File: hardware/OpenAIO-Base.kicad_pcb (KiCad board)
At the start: 6 copper layers, 35 x 35 mm, 341 parts, among them J15 5V, J16 5V, J17 5V, J18 5V, J20 5V, J21 5V, J23 5V, J24 5V, J25 5V, J26 5V, J27 5V, J28 5V, J29 5V, J30 5V, J31 5V, J32 5V, J33 5V, J34 5V, J35 5V, J37 5V, J38 5V, J39 5V, J40 5V, J41 5V, J42 5V, J43 5V, J44 5V, J45 5V, J48 5V, J49 5V, J50 5V, J51 5V, J52 5V, J53 5V, J54 5V, J55 5V, J90 Core_LGA, J91 Core_LGA, Q1 AP1606, Q10 DOY180N03T, Q11 DOY180N03T, Q12 DOY180N03T, Q13 DOY180N03T, Q14 DOY180N03T, Q15 DOY180N03T, Q16 DOY180N03T, Q17 DOY180N03T, Q18 DOY180N03T, Q19 DOY180N03T, Q2 AP1606, Q20 DOY180N03T, Q21 DOY180N03T, Q22 DOY180N03T, Q23 DOY180N03T, Q24 DOY180N03T, Q25 DOY180N03T, Q26 DOY180N03T, Q3 DOY180N03T, Q4 DOY180N03T, Q5 DOY180N03T, Q6 DOY180N03T, Q7 DOY180N03T, Q8 DOY180N03T, Q9 DOY180N03T, U1 TS2306A 240GF MSM 9_C2976675, U10 COS8051SOT, U11 TLV7031DPWR, U12 SM06B-SRSS-TB(LF)(SN), U13 AT32F421G8U7, U14 NSG2065Q, U15 AT32F421G8U7, U16 NSG2065Q, U17 AT32F421G8U7, U18 NSG2065Q, U19 AT32F421G8U7, U2 RP2354A, U20 NSG2065Q, U21 SX1281IMLTRT, U22 ESP32-C3, U23 TLV75533PDQNR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

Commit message: OpenAIO: two board projects from one schematic via the multiboard plugin, master PCB retired
OpenAIO.kicad_pro keeps the schematic; OpenAIO-Base and OpenAIO-Core are full
projects in the same directory, root schematic symlinked, seeded from the last
split of the master. Own design rules per board (Base 2 oz outer, Core 0.8 mm
1 oz, LGA-only bottom). tools/core_model.py exports the Core VRML/STEP as
J90's 3D model. split_boards, lga_place, lga_rule_area, core_outline and
lga_wire_root are gone with the master.

Co-Authored-By: Claude Fable 5 <noreply@anthropic.com>
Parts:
- removed C1, C11, C12, C13, C14, C2, C29, C30, C32, C34, C35, C5, C6, C7, C8, C9: 100n, Capacitor_SMD:C_0201_0603Metric
- removed C10, C4: 20p, Capacitor_SMD:C_0201_0603Metric
- removed C15, C16, C17, C25, C3: 4.7uF, Capacitor_SMD:C_0402_1005Metric
- removed C27: 22uF, Capacitor_SMD:C_0402_1005Metric
- removed C31: 470p, Capacitor_SMD:C_0201_0603Metric
- removed C33: 1uF, Capacitor_SMD:C_0402_1005Metric
- removed D1: LED_1_Blue, LED_SMD:LED_0402_1005Metric
- removed D7: LED_1_Green, LED_SMD:LED_0402_1005Metric
- removed D8: SDM02U30LP3-7B, lib:X3-DFN0603-2_L0.6-W0.3-RD
- removed J23, J26, J30, J34, J35, J37, J38, J39, J40, J41, J42, J43, J44, J45, J48, J49, J50, J51, J52, J53, J54, J55: 5V, lib:small_pad
- removed J91: Core_LGA, lib:Core_LGA_pads
- removed L1: AOTA-B201610S3R3-101-T, lib:IND-SMD_L2.0-W1.6_AOTA-B201610S3R3-101-T
- removed Q1, Q2: AP1606, lib:DFN-3L_L1.0-W0.6-P0.65-BR
- removed R1, R13: 100k, Resistor_SMD:R_0201_0603Metric
- removed R10, R8, R9: 30R, Resistor_SMD:R_0201_0603Metric
- removed R11, R12: 5.1k, Resistor_SMD:R_0201_0603Metric
- removed R14: 2.4k, Resistor_SMD:R_0201_0603Metric
- removed R15, R16, R26, R33: 75R, Resistor_SMD:R_0201_0603Metric
- removed R2, R25, R7: 10k, Resistor_SMD:R_0201_0603Metric
- removed R23: 6.49k, Resistor_SMD:R_0201_0603Metric
- removed R27: 3.9k, Resistor_SMD:R_0201_0603Metric
- removed R28: 12k, Resistor_SMD:R_0201_0603Metric
- removed R29: 1.4k, Resistor_SMD:R_0201_0603Metric
- removed R30: 680R, Resistor_SMD:R_0201_0603Metric
- removed R31, R32: 510R, Resistor_SMD:R_0201_0603Metric
- removed R5, R6: 1k, Resistor_SMD:R_0201_0603Metric
- removed U1: TS2306A 240GF MSM 9_C2976675, lib:SW-SMD_4P-L3.0-W2.0-P0.85-LS3.5
- removed U10: COS8051SOT, lib:SOT-23-5_L3.0-W1.7-P0.95-LS2.8-BR
- removed U11: TLV7031DPWR, lib:X2SON-4_L0.8-W0.8-P0.48-TL-A
- removed U2: RP2354A, lib:QFN-60_L7.0-W7.0-P0.40-TL-EP3.4
- removed U6: LP5912-1.8DRVR, lib:WSON-6-1EP_2x2mm_P0.65mm_EP1x1.6mm_ThermalVias
- removed U8: BMI270, lib:LGA-14_L3.0-W2.5-P0.50-BR
- removed U9: SN74LVC1G3157DTBR, lib:X2SON-6_L1.0-W0.8-BL
- removed X1: XTM25012000JT00351001, lib:CRYSTAL-SMD_4P-L2.5-W2.0-BL-A
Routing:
- net /OSD/VIDEO_IN: track 2.65 -> 0.00 mm
- net GND: track 20.3 -> 17.7 mm
- net /OSD/VID_FILT: track 2.57 -> 0.00 mm
- net /RP2354A/XIN: track 2.45 -> 0.00 mm
- net +3.3V: track 2.43 -> 0.00 mm
- net /OSD/VID_DC: track 1.47 -> 0.00 mm
- net Net-(C10-Pad2): track 0.88 -> 0.00 mm
- net /OSD/OSD_LVL: track 0.65 -> 0.00 mm
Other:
- board text added: "AIO"
- board text added: "Open"

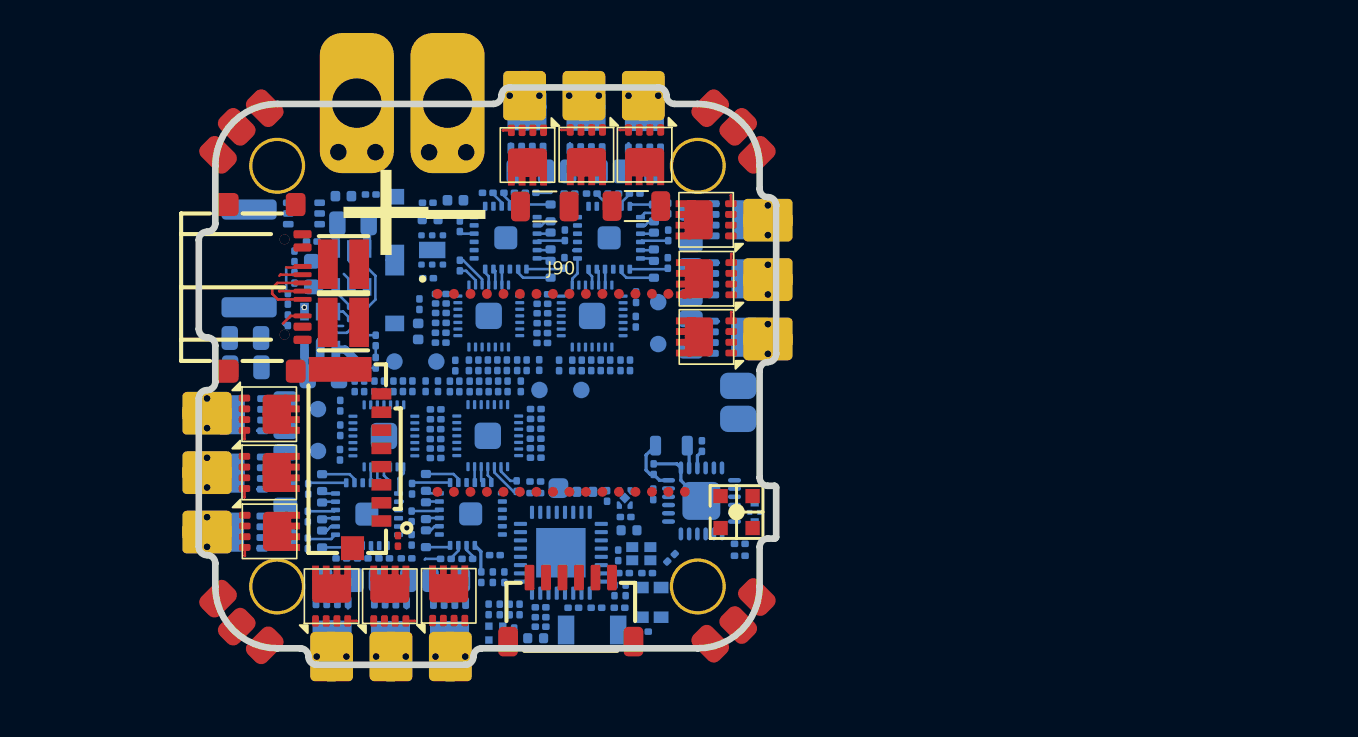
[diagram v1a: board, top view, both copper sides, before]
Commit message: OpenAIO: test points TP10-TP30 as LGA position markers (schematic + Base), project files as re-saved by KiCad
Co-Authored-By: Claude Fable 5 <noreply@anthropic.com>
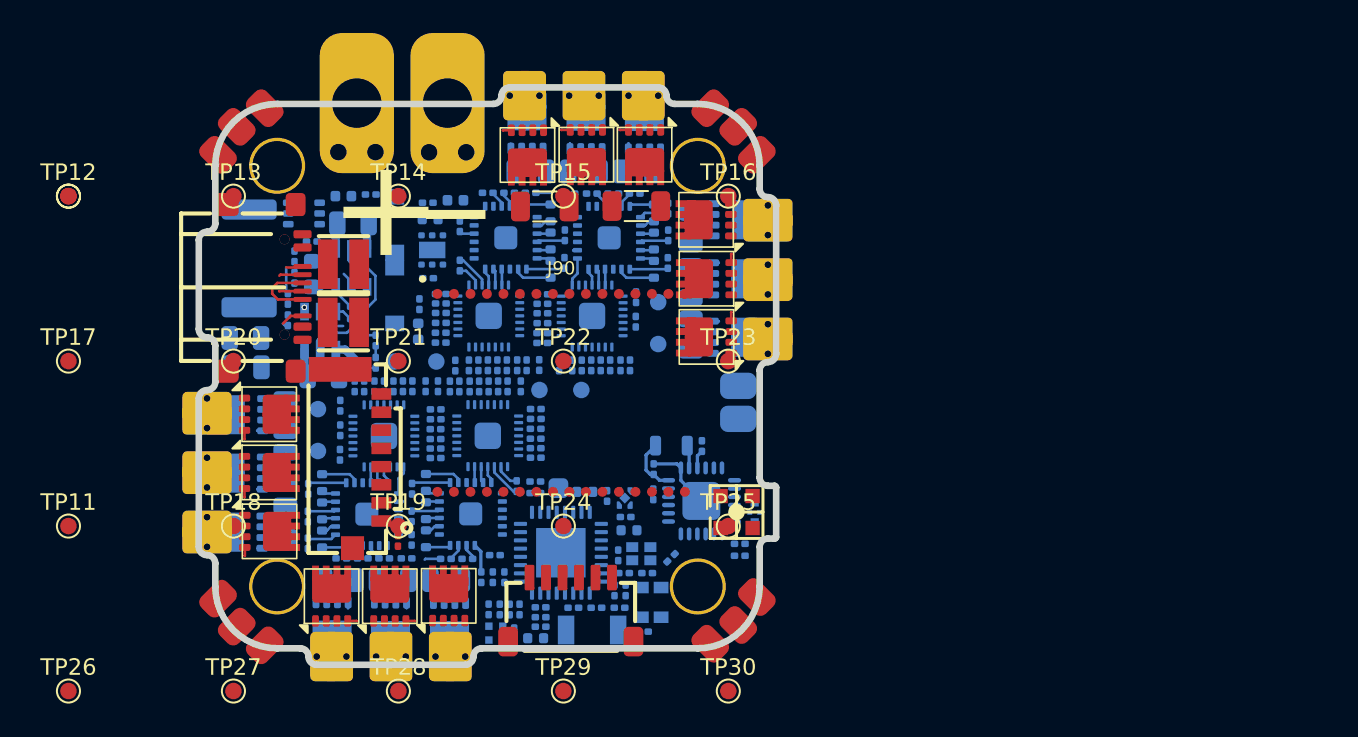
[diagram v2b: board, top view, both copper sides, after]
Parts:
- added TP10: TestPoint, OpenDrone:TestPoint_Pad_D1.0mm, F.Cu at (50.0, 50.0)
- added TP11: TestPoint, TestPoint:TestPoint_Pad_D1.0mm, F.Cu at (50.0, 70.0)
- added TP12: TestPoint, TestPoint:TestPoint_Pad_D1.0mm, F.Cu at (50.0, 50.0)
- added TP13: TestPoint, TestPoint:TestPoint_Pad_D1.0mm, F.Cu at (60.0, 50.0)
- added TP14: TestPoint, TestPoint:TestPoint_Pad_D1.0mm, F.Cu at (70.0, 50.0)
- added TP15: TestPoint, TestPoint:TestPoint_Pad_D1.0mm, F.Cu at (80.0, 50.0)
- added TP16: TestPoint, TestPoint:TestPoint_Pad_D1.0mm, F.Cu at (90.0, 50.0)
- added TP17: TestPoint, TestPoint:TestPoint_Pad_D1.0mm, F.Cu at (50.0, 60.0)
- added TP18: TestPoint, TestPoint:TestPoint_Pad_D1.0mm, F.Cu at (60.0, 70.0)
- added TP19: TestPoint, TestPoint:TestPoint_Pad_D1.0mm, F.Cu at (70.0, 70.0)
- added TP20: TestPoint, TestPoint:TestPoint_Pad_D1.0mm, F.Cu at (60.0, 60.0)
- added TP21: TestPoint, TestPoint:TestPoint_Pad_D1.0mm, F.Cu at (70.0, 60.0)
- added TP22: TestPoint, TestPoint:TestPoint_Pad_D1.0mm, F.Cu at (80.0, 60.0)
- added TP23: TestPoint, TestPoint:TestPoint_Pad_D1.0mm, F.Cu at (90.0, 60.0)
- added TP24: TestPoint, TestPoint:TestPoint_Pad_D1.0mm, F.Cu at (80.0, 70.0)
- added TP25: TestPoint, TestPoint:TestPoint_Pad_D1.0mm, F.Cu at (90.0, 70.0)
- added TP26: TestPoint, TestPoint:TestPoint_Pad_D1.0mm, F.Cu at (50.0, 80.0)
- added TP27: TestPoint, TestPoint:TestPoint_Pad_D1.0mm, F.Cu at (60.0, 80.0)
- added TP28: TestPoint, TestPoint:TestPoint_Pad_D1.0mm, F.Cu at (70.0, 80.0)
- added TP29: TestPoint, TestPoint:TestPoint_Pad_D1.0mm, F.Cu at (80.0, 80.0)
- added TP30: TestPoint, TestPoint:TestPoint_Pad_D1.0mm, F.Cu at (90.0, 80.0)

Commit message: OpenAIO: LGA pins from Stan's marker test points, 30 pads, J90/J91 regenerated and placed
lga_gen.py --from-base reads the marker test points on the Base (position +
net) into its pin table and generates footprints, symbol and interface
sheet; lga_apply.py replaces the markers with J90 at the pattern centre and
J91 on the Core, marks the marker symbols exclude-from-board and adds the
LED_STRIP global label on the root (it now crosses the LGA). Plugin update
assigned all 30 pad nets on both boards.

Co-Authored-By: Claude Fable 5 <noreply@anthropic.com>
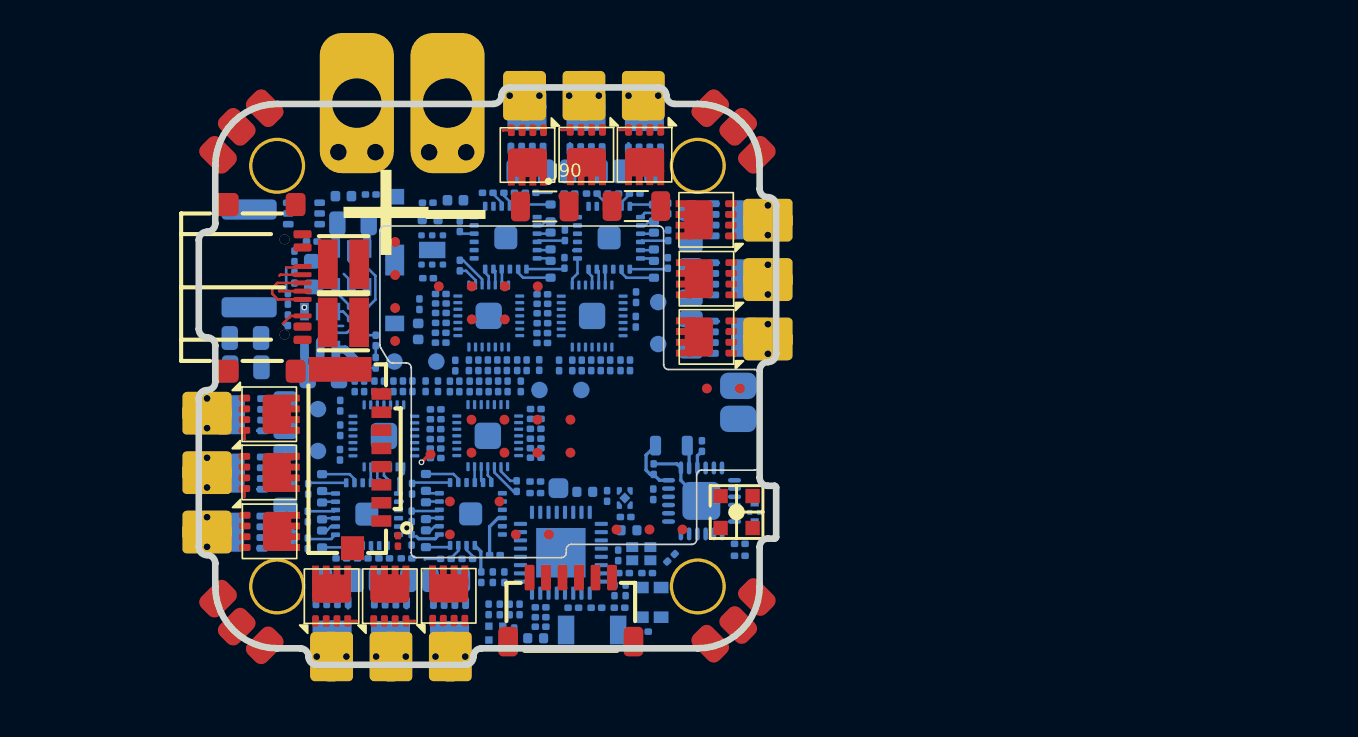
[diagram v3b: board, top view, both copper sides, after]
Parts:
- removed TP10: TestPoint, OpenDrone:TestPoint_Pad_D1.0mm
- removed TP11, TP12, TP13, TP14, TP15, TP16, TP17, TP18, TP19, TP20, TP21, TP22, TP23, TP24, TP25, TP26, TP27, TP28, TP29, TP30: TestPoint, TestPoint:TestPoint_Pad_D1.0mm
- moved J90 1.71 mm to (80.2, 60.3)
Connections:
- J20 pad 1: /Pads/LED_STRIP -> LED_STRIP
- J21 pad 1: /Pads/LED_STRIP -> LED_STRIP
- J31 pad 1: /Pads/LED_STRIP -> LED_STRIP
- J32 pad 1: /Pads/LED_STRIP -> LED_STRIP
- J90 pad 10: +3.3V -> GND
- J90 pad 11: +3.3V -> USB_D-
- J90 pad 12: +4v5 -> GND
- J90 pad 14: 10V_ENABLE -> MOTOR2
- J90 pad 15: CURR -> MOTOR4
- J90 pad 18: USB_D+ -> MOTOR1
- J90 pad 19: USB_D- -> MOTOR3
- J90 pad 2: +BATT -> 10V_ENABLE
- J90 pad 21: MOTOR1 -> GND
- J90 pad 22: MOTOR2 -> +BATT
- J90 pad 23: MOTOR3 -> GND
- J90 pad 24: MOTOR4 -> GND
- J90 pad 25: UART0_TX -> GND
- J90 pad 26: UART0_RX -> UART0_TX
- J90 pad 27: UART1_TX -> UART0_RX
- J90 pad 28: UART1_RX -> LED_STRIP
- J90 pad 29: SPI0.SCK -> UART1_RX
- J90 pad 3: GND -> CURR
- J90 pad 30: SPI0.MOSI -> UART1_TX
- J90 pad 4: +5V -> SPI0.MISO
- J90 pad 5: +5V -> SPI0.SCK
- J90 pad 6: GND -> SPI0.MOSI
- J90 pad 7: +10V -> FLASH_CS
- J90 pad 8: +10V -> USB_D+
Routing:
- net +10V: track 2.01 -> 4.58 mm
- net /ESC2/GHC: track 0.00 -> 1.57 mm
- net +BATT: track 4.27 -> 5.02 mm, vias 0 -> 1
- net Net-(Q21-G): track 0.54 -> 0.00 mm
- net Net-(Q23-G): track 0.56 -> 0.03 mm
- net Net-(Q7-G): track 0.52 -> 0.01 mm
- net Net-(Q25-G): track 0.52 -> 0.01 mm
